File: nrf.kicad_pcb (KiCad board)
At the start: 2 copper layers, 35.6 x 35.6 mm, 56 parts, among them IC1 BMA423, IC2 113990582, J2 Conn_01x05, J7 Conn_01x12, Q1 SI3139K, Q2 MGSF1N02L, Q3 SI3139K, Q4 SI3139K, SW1 UP, SW2 MID, SW3 DOWN, SW4 RESET, SW5 BACK, U1 GD25Q16, U2 C0720B001F, U3 MCP73871-xxI_ML, U4 MIC5219-3.3YM5, X1 32.768

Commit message: Board Update
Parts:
- removed R18, R19: 10K, Resistors_SMD:R_0603_HandSoldering
- removed SW4: RESET, Buttons_Switches_SMD:SW_SPST_B3U-1000P
- added L1: 10uH, Inductor_SMD:L_0603_1608Metric_Pad1.05x0.95mm_HandSolder, F.Cu at (139.6, 117.0)
- added R20: 1M, Resistor_SMD:R_0201_0603Metric_Pad0.64x0.40mm_HandSolder, F.Cu at (132.4, 102.2)
- added R21: 1M, Resistor_SMD:R_0201_0603Metric_Pad0.64x0.40mm_HandSolder, F.Cu at (132.4, 103.1)
- C1, C10, C11, C12, C13, C14, C2, C3, C4, C5, C6, C8: footprint Capacitors_SMD:C_0603_HandSoldering -> Capacitor_SMD:C_0201_0603Metric_Pad0.64x0.40mm_HandSolder
- C7: value 470pF -> 0.1uF; footprint Capacitors_SMD:C_0603_HandSoldering -> Capacitor_SMD:C_0201_0603Metric_Pad0.64x0.40mm_HandSolder
- C9: value 470pF -> 4.7uF; footprint Capacitors_SMD:C_0603_HandSoldering -> Capacitor_SMD:C_0201_0603Metric_Pad0.64x0.40mm_HandSolder
- IC2: footprint SamacSys_Parts:113990582 -> RF_Module:Raytac_MDBT50Q
- R1, R10, R11, R12, R13, R14, R15, R16, R17, R2, R3, R4, R5, R6, R7, R8, R9: footprint Resistors_SMD:R_0603_HandSoldering -> Resistor_SMD:R_0201_0603Metric_Pad0.64x0.40mm_HandSolder
- SW1, SW2, SW3, SW5: moved to B.Cu
- TP1, TP2, TP3: footprint Measurement_Points:Measurement_Point_Square-SMD-Pad_Big -> TestPoint:TestPoint_Pad_2.0x2.0mm
- TP4: footprint Measurement_Points:Measurement_Point_Square-SMD-Pad_Big -> TestPoint:TestPoint_Pad_2.0x2.0mm; moved to B.Cu
- moved C8 37.1 mm to (138.4, 94.5), turned to 90 degrees
- moved TP3 33.2 mm to (126.0, 114.8)
- moved J2 33.2 mm to (149.2, 124.0), turned to 295 degrees
- moved TP1 31.7 mm to (136.7, 120.0)
- moved TP2 29.4 mm to (144.0, 120.0)
- moved C12 28.7 mm to (110.7, 114.8)
- moved Q2 28.7 mm to (108.2, 115.7)
- moved D4 28.7 mm to (108.3, 112.7)
- moved R17 28.7 mm to (105.8, 114.2)
- moved R1 28.7 mm to (107.6, 111.3), turned to 0 degrees
- moved TP4 25.9 mm to (126.0, 105.2)
- moved U2 23.8 mm to (107.1, 106.5)
- moved R4 18.9 mm to (133.8, 108.8), turned to 270 degrees
- moved R16 18.7 mm to (131.9, 112.9), turned to 270 degrees
- moved C3 17.5 mm to (129.2, 105.5), turned to 90 degrees
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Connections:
- IC2 pad 11: Net-(IC2-Pad11) -> /BATT_LVL
- IC2 pad 16: Net-(IC2-Pad16) -> /PWR_CHRGING
- IC2 pad 20: /BTN_1 -> Net-(IC2-Pad20)
- IC2 pad 22: /BTN_2 -> Net-(IC2-Pad22)
- IC2 pad 24: /BTN_3 -> Net-(IC2-Pad24)
- IC2 pad 27: Net-(IC2-Pad27) -> /INT1
- IC2 pad 31: /INT1 -> Net-(IC2-Pad31)
- IC2 pad 32: (GND) -> Net-(IC2-Pad32)
- IC2 pad 37: Net-(IC2-Pad37) -> /BTN_2
- IC2 pad 39: /PWR_CHRGING -> /BTN_3
- IC2 pad 9: Net-(IC2-Pad9) -> /BTN_1
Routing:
- net +5: track 6.47 -> 35.5 mm, vias 0 -> 4
- net /BTN_1: track 0.00 -> 25.4 mm, vias 0 -> 1
- net /BTN_2: track 0.00 -> 25.0 mm, vias 0 -> 1
- net /BATT_LVL: track 0.00 -> 19.1 mm, vias 0 -> 2
- net /BTN_3: track 0.00 -> 18.5 mm, vias 0 -> 1
- net /SWDIO: track 0.00 -> 14.6 mm, vias 0 -> 1
- net /SPI_RESET: track 0.00 -> 14.2 mm, vias 0 -> 1
- net /SWDCLK: track 0.00 -> 14.1 mm, vias 0 -> 1
- net /RESET: track 0.00 -> 13.3 mm, vias 0 -> 2
- net /LEDA: track 7.51 -> 20.7 mm, vias 0 -> 4
- net /BATT: track 3.72 -> 16.3 mm, vias 0 -> 1
- net /VOUT: track 12.5 -> 24.1 mm
- net +3.3: track 9.09 -> 18.2 mm, vias 1 -> 2
- net /PWR_CHRGING: track 2.51 -> 11.3 mm, vias 0 -> 2
- net /SDA: track 23.9 -> 15.9 mm
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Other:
- board size 35.6 x 35.6 mm -> 54 x 35.6 mm

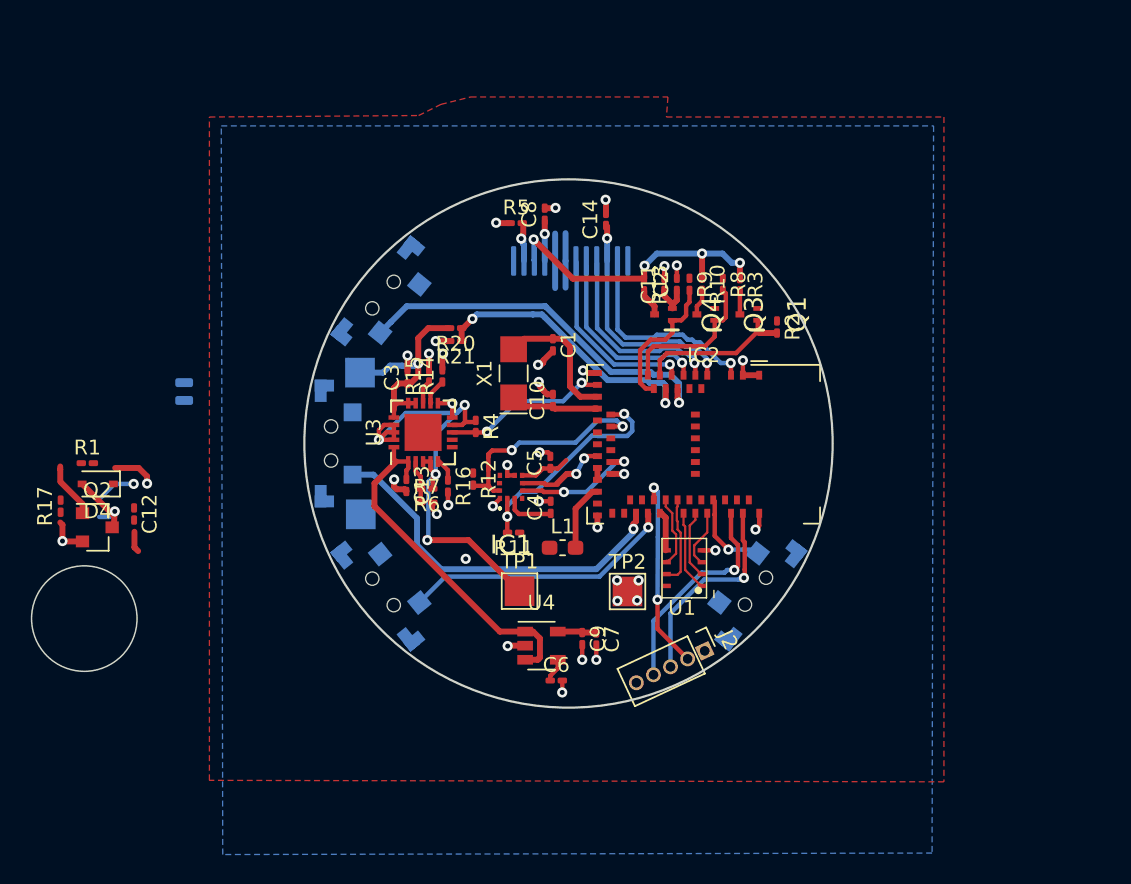
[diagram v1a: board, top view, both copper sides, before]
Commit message: Change resistors to 0603 imperial
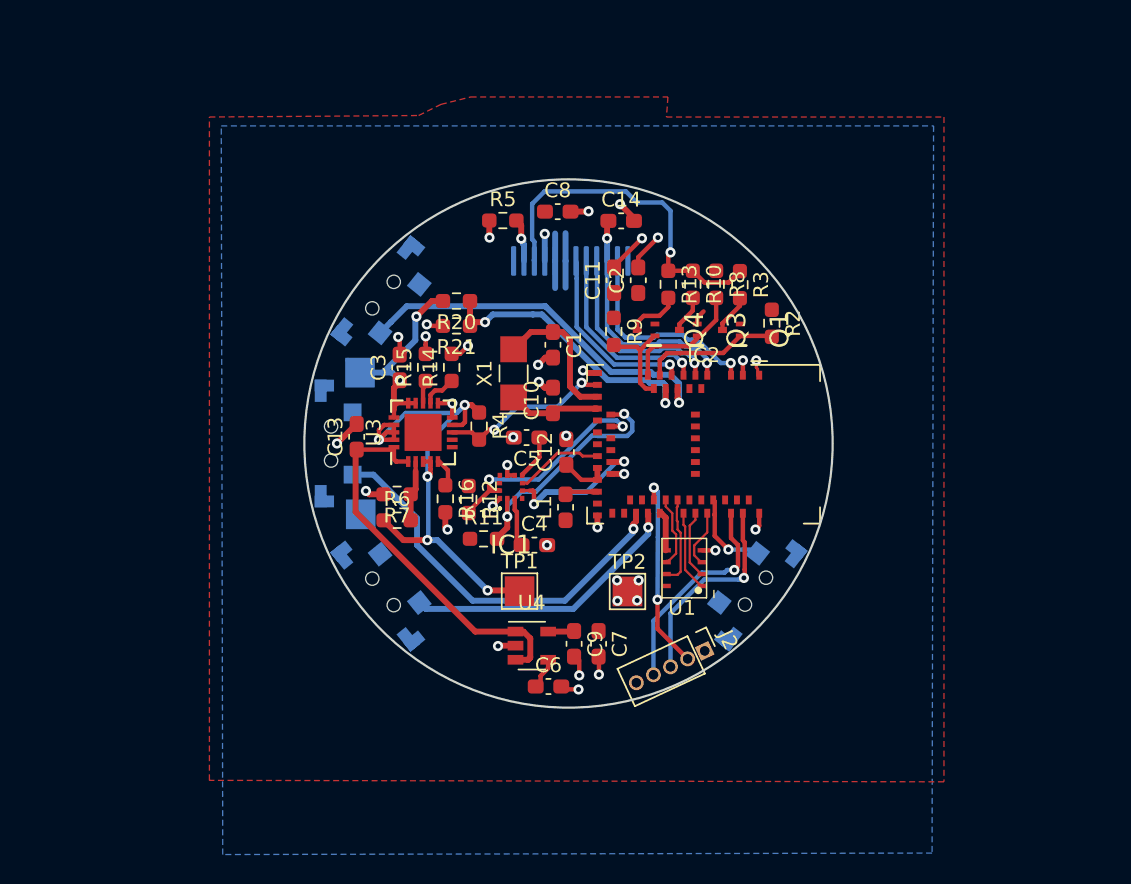
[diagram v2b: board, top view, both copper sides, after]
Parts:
- removed D4: ZLLS410, Diodes_SMD:D_SOD-323
- removed Q2: MGSF1N02L, TO_SOT_Packages_SMD:SOT-23
- removed R1: 330, Resistor_SMD:R_0201_0603Metric_Pad0.64x0.40mm_HandSolder
- removed R17: 10K, Resistor_SMD:R_0201_0603Metric_Pad0.64x0.40mm_HandSolder
- removed U2: C0720B001F, my-fp-library:VIBRATION MOTOR COIN 3V FLEX - C0720B001F
- C1, C10, C11, C12, C13, C14, C2, C3, C4, C5, C6, C7, C8, C9: footprint Capacitor_SMD:C_0201_0603Metric_Pad0.64x0.40mm_HandSolder -> Capacitor_SMD:C_0603_1608Metric_Pad1.08x0.95mm_HandSolder
- R10, R11, R12, R13, R14, R15, R16, R2, R20, R21, R3, R4, R5, R6, R7, R8, R9: footprint Resistor_SMD:R_0201_0603Metric_Pad0.64x0.40mm_HandSolder -> Resistor_SMD:R_0603_1608Metric_Pad0.98x0.95mm_HandSolder
- moved C12 29.4 mm to (139.8, 110.6), turned to 90 degrees
- moved R9 6.01 mm to (143.1, 102.5)
- moved C13 4.68 mm to (125.7, 109.5), turned to 90 degrees
- moved C11 3.39 mm to (143.1, 99.0)
- moved R6 2.92 mm to (128.4, 115.2), turned to 0 degrees
- moved C4 2.78 mm to (137.7, 116.8), turned to 0 degrees
- moved L1 2.73 mm to (139.8, 114.3), turned to 90 degrees
- moved C2 2.61 mm to (144.7, 99.0)
- moved C5 2.32 mm to (137.2, 109.6), turned to 180 degrees
- moved R7 2.07 mm to (128.4, 113.4), turned to 180 degrees
- moved R11 2.07 mm to (134.3, 116.4), turned to 0 degrees
- moved R20 1.83 mm to (132.4, 100.4)
- moved R13 1.63 mm to (146.7, 99.3)
- moved Q1 1.58 mm to (151.0, 102.3)
- moved Q3 1.58 mm to (148.1, 102.3)
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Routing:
- net Net-(D4-Pad2): track 5.74 -> 0.00 mm, vias 1 -> 0
- net +3.3: track 18.2 -> 14.2 mm, vias 2 -> 1
- net Net-(Q2-Pad1): track 3.71 -> 0.00 mm
- net /LIGHT2: track 9.79 -> 6.56 mm
- net /LEDA: track 20.7 -> 23.8 mm, vias 4 -> 1
- net /MOTOR_PWM: track 3.77 -> 0.90 mm, vias 2 -> 1
- net +5: track 35.5 -> 38.2 mm, vias 4 -> 5
- net /VOUT: track 24.1 -> 26.5 mm
- net Net-(IC2-Pad31): track 4.58 -> 2.22 mm
- net Net-(Q4-Pad3): track 1.88 -> 3.65 mm
- net /BTN_2: track 25.0 -> 26.8 mm
- net /LIGHT1: track 10.3 -> 8.66 mm
- net /XL1: track 9.13 -> 10.8 mm
- net /LIGHT3: track 10.5 -> 9.26 mm
- net Net-(R6-Pad2): track 2.90 -> 4.10 mm
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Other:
- board size 54 x 35.6 mm -> 35.6 x 35.6 mm

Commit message: Board Update
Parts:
- added 3.3: , TestPoint:TestPoint_Pad_D1.0mm, F.Cu at (131.9, 96.2)
- added GND: , TestPoint:TestPoint_Pad_D1.0mm, F.Cu at (131.8, 98.3)
- added PWM: , TestPoint:TestPoint_Pad_D1.0mm, F.Cu at (133.7, 97.1)
- Q1, Q3, Q4: footprint TO_SOT_Packages_SMD:SOT-723_Handsoldering -> Package_TO_SOT_SMD:SOT-723
- turned Q1 to 180 degrees
- turned Q3 to 180 degrees
- turned Q4 to 180 degrees
- renumbered TP1 to +5, TP4 to BATT, TP3 to GND, TP2 to GND
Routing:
- net /MOTOR_PWM: track 0.90 -> 22.8 mm, vias 1 -> 3
- net (GND): track 42.2 -> 47.5 mm, vias 34 -> 35
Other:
- board text added: "3.3"
- board text added: "CLK"
- board text added: "GND"
- board text added: "IO"
- board text added: "RST"

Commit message: Board Update
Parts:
- moved R5 9.86 mm to (145.4, 94.5), turned to 180 degrees
- moved C14 7.27 mm to (136.3, 94.4), turned to 180 degrees
- moved C8 2.05 mm to (141.3, 94.4), turned to 180 degrees
- turned J7 to 0 degrees
- renumbered +5 to TP1, GND to TP2, GND to TP3, BATT to TP4, PWM to TP5, 3.3 to TP6, GND to TP7
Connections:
- IC2 pad 10: /SPI_DC -> /SPI_RESET
- IC2 pad 3: /SPI_RESET -> /SPI_DC
- IC2 pad 4: /SPI_MOSI -> /SPI_CS
- IC2 pad 8: /SPI_CS -> /SPI_MOSI
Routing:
- net /LEDA: track 23.8 -> 17.3 mm
- net /SPI_MOSI: track 15.7 -> 19.5 mm
- net +3.3: track 14.2 -> 17.8 mm
- net /SPI_DC: track 12.5 -> 15.6 mm
- net /SPI_CS: track 12.7 -> 14.9 mm
- net /SPI_SCK: track 13.2 -> 14.8 mm
- net Net-(J7-Pad2): track 3.07 -> 3.78 mm
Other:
- board text added: "5V"
- board text added: "BATT"
- board text added: "PWM"

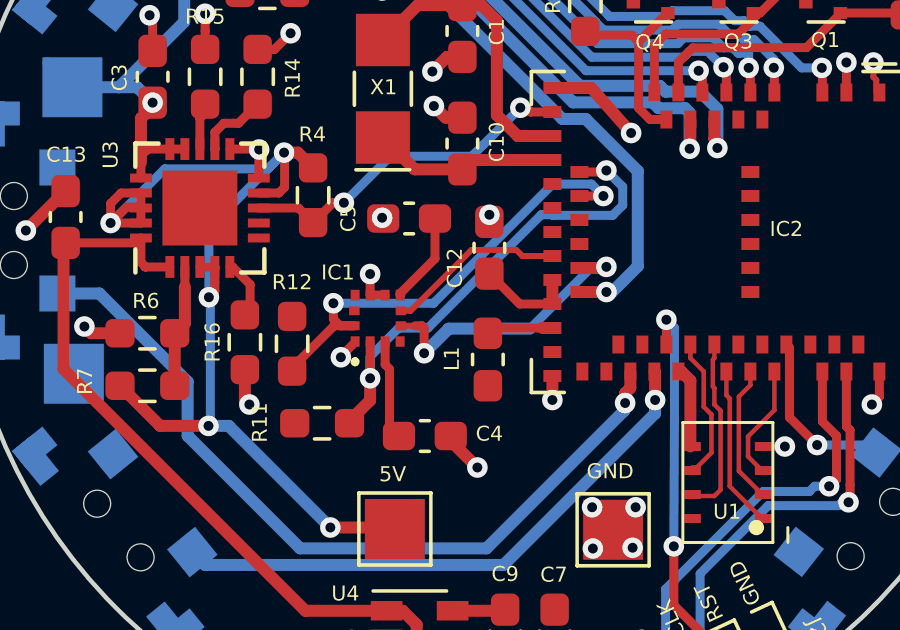
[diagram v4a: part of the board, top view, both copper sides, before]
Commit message: Update footprints
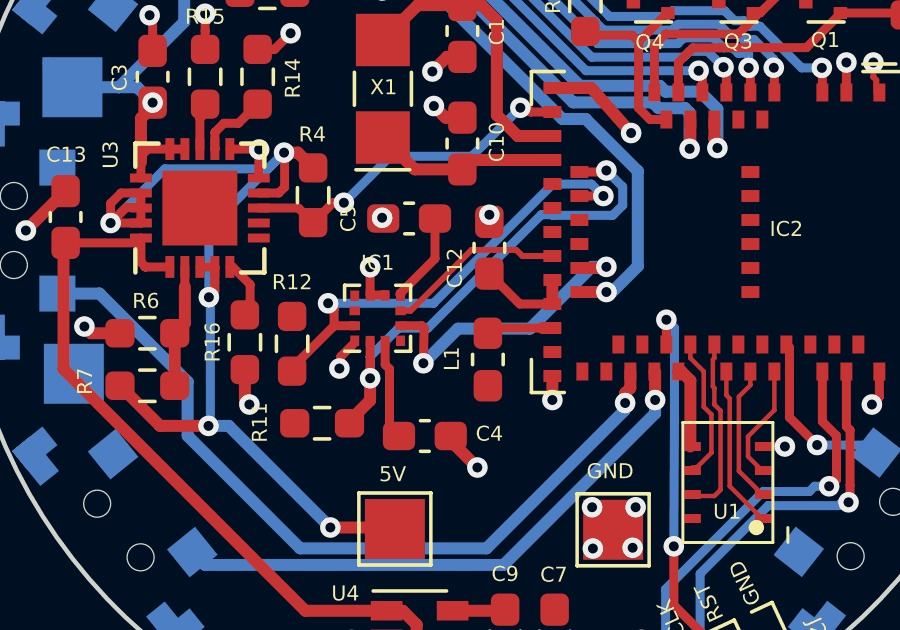
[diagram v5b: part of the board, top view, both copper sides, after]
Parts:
- IC1: footprint SamacSys_Parts:BMA423 -> Package_LGA_marks:LGA-12_2x2mm_P0.5mm_small_pad
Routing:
- net (GND): track 47.6 -> 48.2 mm
- net /INT1: track 9.85 -> 10.4 mm

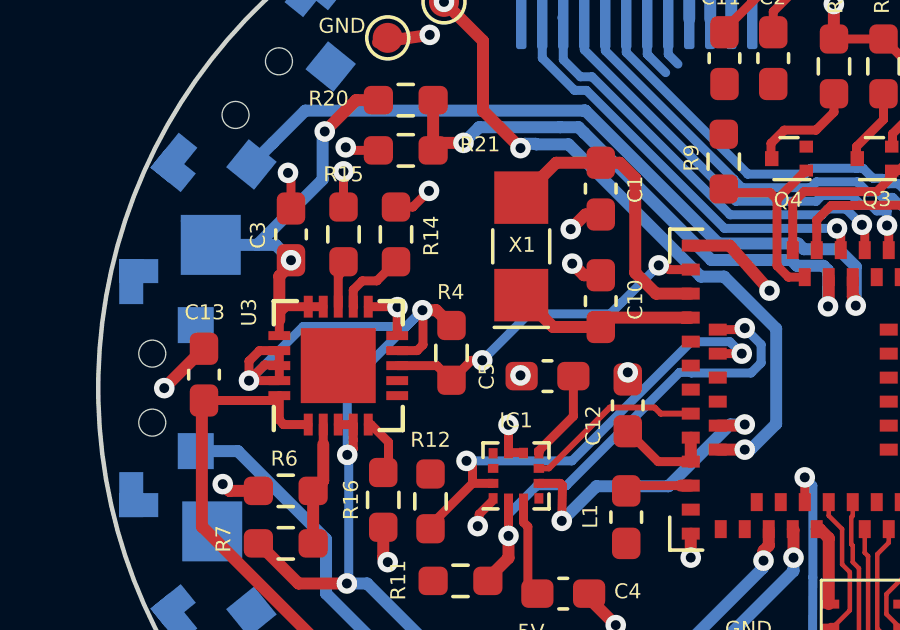
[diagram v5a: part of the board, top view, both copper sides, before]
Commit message: Update GND connections from under pads
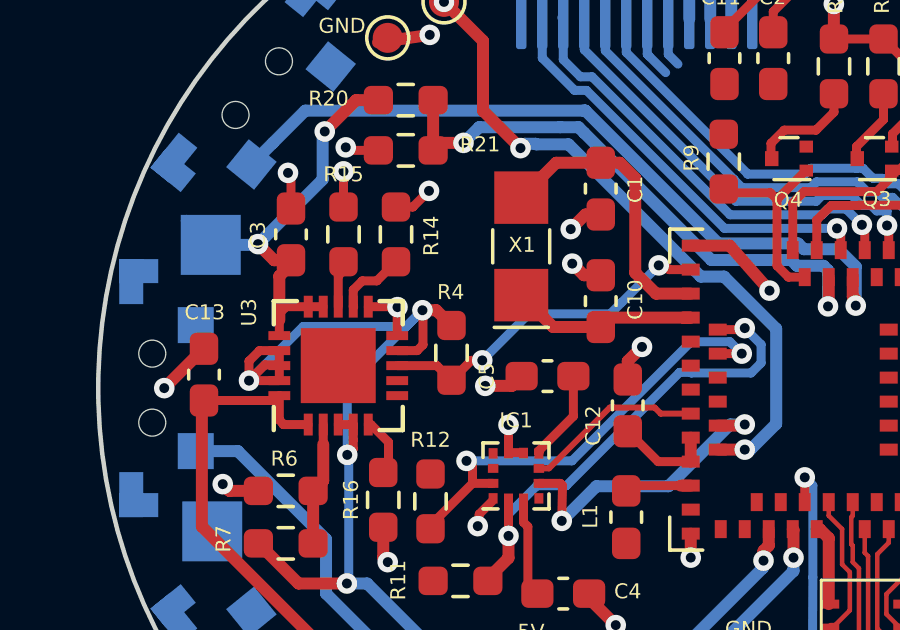
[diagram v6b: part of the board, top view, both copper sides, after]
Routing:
- net (GND): track 48.2 -> 50.8 mm

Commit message: Board updates
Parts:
- removed TP5, TP6, TP7: , TestPoint:TestPoint_Pad_D1.0mm
- added D4: ZLLS410, Diode_SMD:D_SOD-323_HandSoldering, B.Cu at (132.7, 122.5)
- added Q2: MGSF1N02L, Package_TO_SOT_SMD:SOT-23, B.Cu at (136.8, 125.2)
- added R1: 330, Resistor_SMD:R_0603_1608Metric_Pad0.98x0.95mm_HandSolder, B.Cu at (141.2, 123.8)
- added R17: 10K, Resistor_SMD:R_0603_1608Metric_Pad0.98x0.95mm_HandSolder, B.Cu at (139.5, 125.2)
- added U2: C0720B001F, Package_LGA_marks:VIBRATION MOTOR COIN 3V FLEX - C0720B001F, B.Cu at (131.8, 131.2)
- TP1, TP2: footprint TestPoint:TestPoint_Pad_2.0x2.0mm -> TestPoint:TestPoint_Pad_D1.5mm
- moved TP1 3.14 mm to (139.8, 119.6)
- moved TP2 1.64 mm to (142.4, 119.6)
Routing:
- net /MOTOR_PWM: track 22.8 -> 14.9 mm
- net Net-(D4-Pad2): track 0.00 -> 7.43 mm
- net Net-(Q2-Pad1): track 0.00 -> 3.65 mm
- net +3.3: track 17.8 -> 21.2 mm, vias 1 -> 3
- net +5: track 38.2 -> 41.4 mm
- net (GND): track 50.8 -> 52.0 mm, vias 35 -> 32
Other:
- outline, holes or cut-outs redrawn
- board text removed: "PWM"
